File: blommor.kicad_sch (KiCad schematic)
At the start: 43 parts

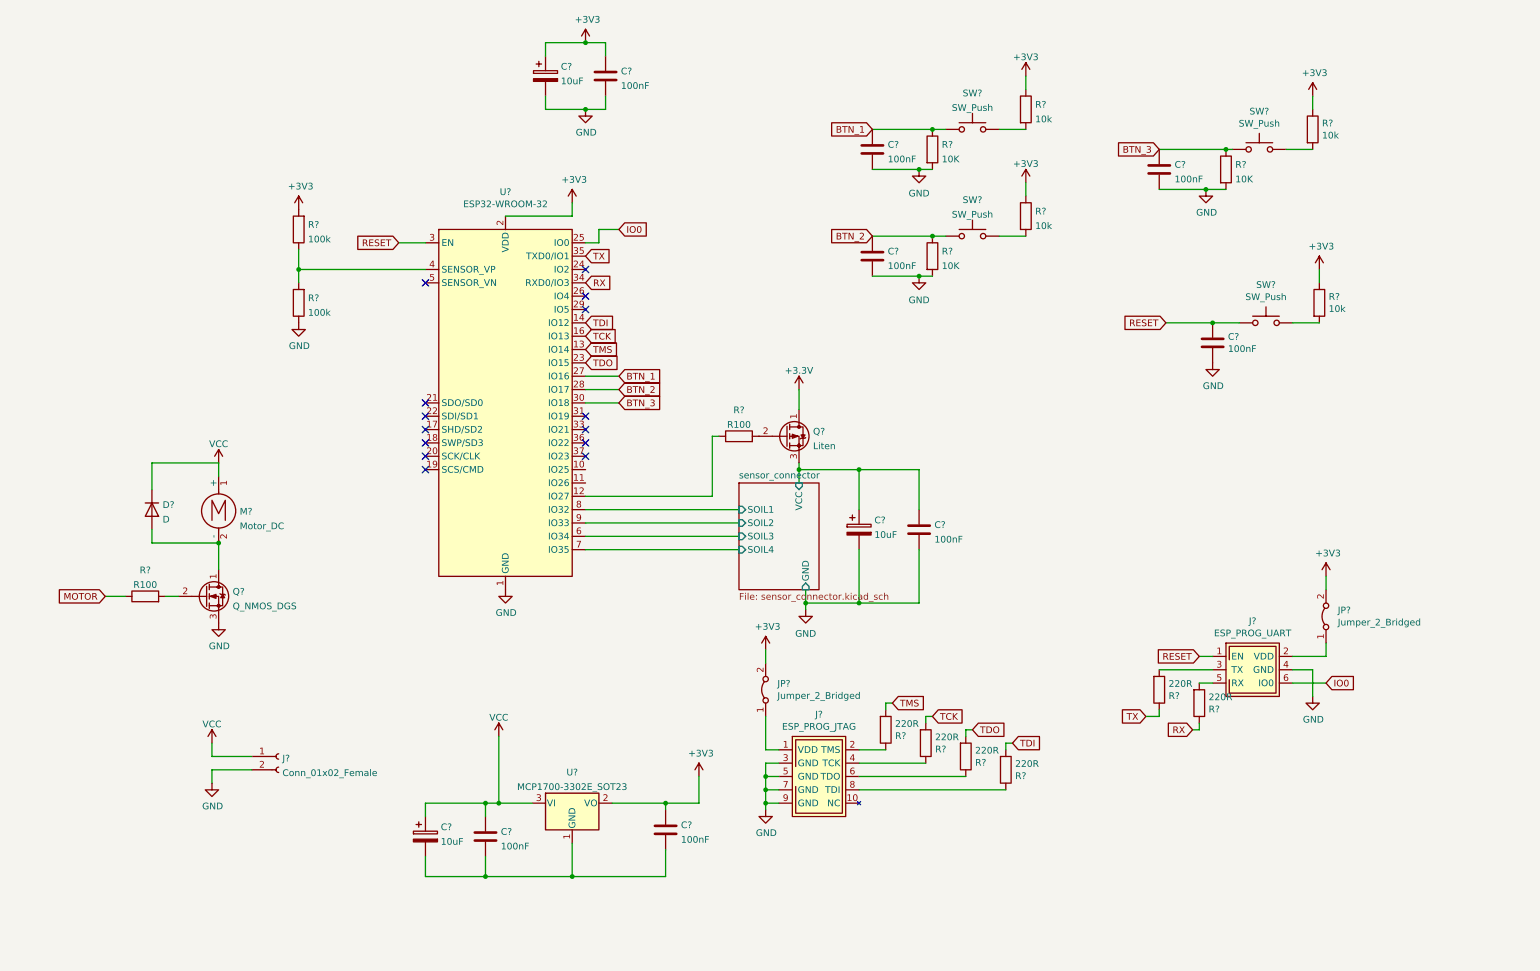
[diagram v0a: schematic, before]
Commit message: Added Amplifier board om "special" lib. Added Amplifier to board with shutdown pins. Added DHT11 sensor to sensor schematic. Updated connector lib.
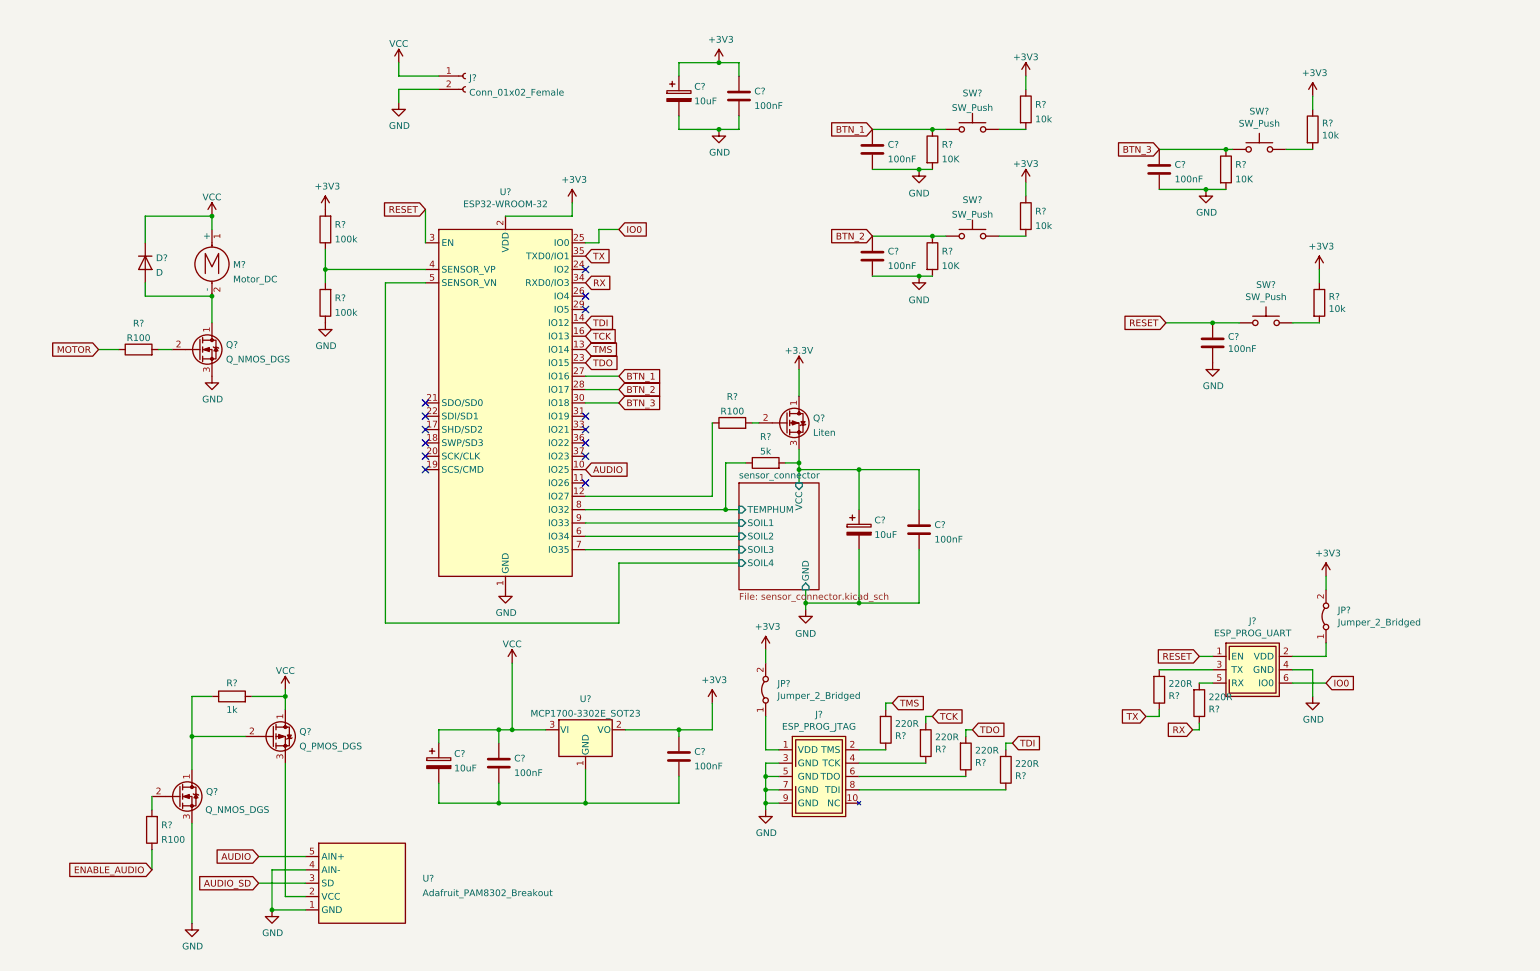
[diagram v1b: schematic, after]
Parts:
- removed SW?: SW_Push, Button_Switch_SMD:SW_SPST_TL3342, symbol Switch:SW_Push
- added Q?: Q_PMOS_DGS, symbol Device:Q_PMOS_DGS
- added Q?: Q_NMOS_DGS, symbol Device:Q_NMOS_DGS
- added R?: 1k, symbol Device:R
- added R?: 5k, symbol Device:R
- added R?: R100, symbol Device:R
- added SW?: SW_Push, Button_Switch_THT:SW_PUSH_6mm_H5mm, symbol Switch:SW_Push
- added U?: Adafruit_PAM8302_Breakout, special:Adafruit_PAM8302_Breakout, symbol special:Adafruit_PAM8302_Breakout
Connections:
- net GND: now also Q?.3 (S), U?.1 (GND), U?.4 (AIN-)
- net RESET: now also SW?.1
- net VCC: now also Q?.1 (D), R?.2
- net sensor_connector/SOIL1: now also U?.9 (IO33); no longer U?.8 (IO32)
- net sensor_connector/SOIL2: now also U?.6 (IO34); no longer U?.9 (IO33)
- net sensor_connector/SOIL3: now also U?.7 (IO35); no longer U?.6 (IO34)
- net sensor_connector/SOIL4: now also U?.5 (SENSOR_VN); no longer U?.7 (IO35)
- net sensor_connector/VCC: now also R?.2
- net at R?.2: now also SW?.2
- net AUDIO: now reaches U?.10 (IO25)
- net AUDIO: now also U?.5 (AIN+)
- new net: Q?.1 (D), Q?.2 (G), R?.1
- new net: Q?.2 (G), R?.2
- new net: Q?.3 (S), U?.2 (VCC)
- new net AUDIO_SD: U?.3 (SD)
- new net ENABLE_AUDIO: R?.1
- new net sensor_connector/TEMPHUM: R?.1, U?.8 (IO32)
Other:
- sheet sensor_connector ports: added TEMPHUM; removed none
- moved on the sheet: C?, D?, J?, M?, Q?, R?, U?

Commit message: Corrected RESET curcit to not keep the device in reset state. Added more capacitors to be a buffer for the motor. Added fuse to motor.
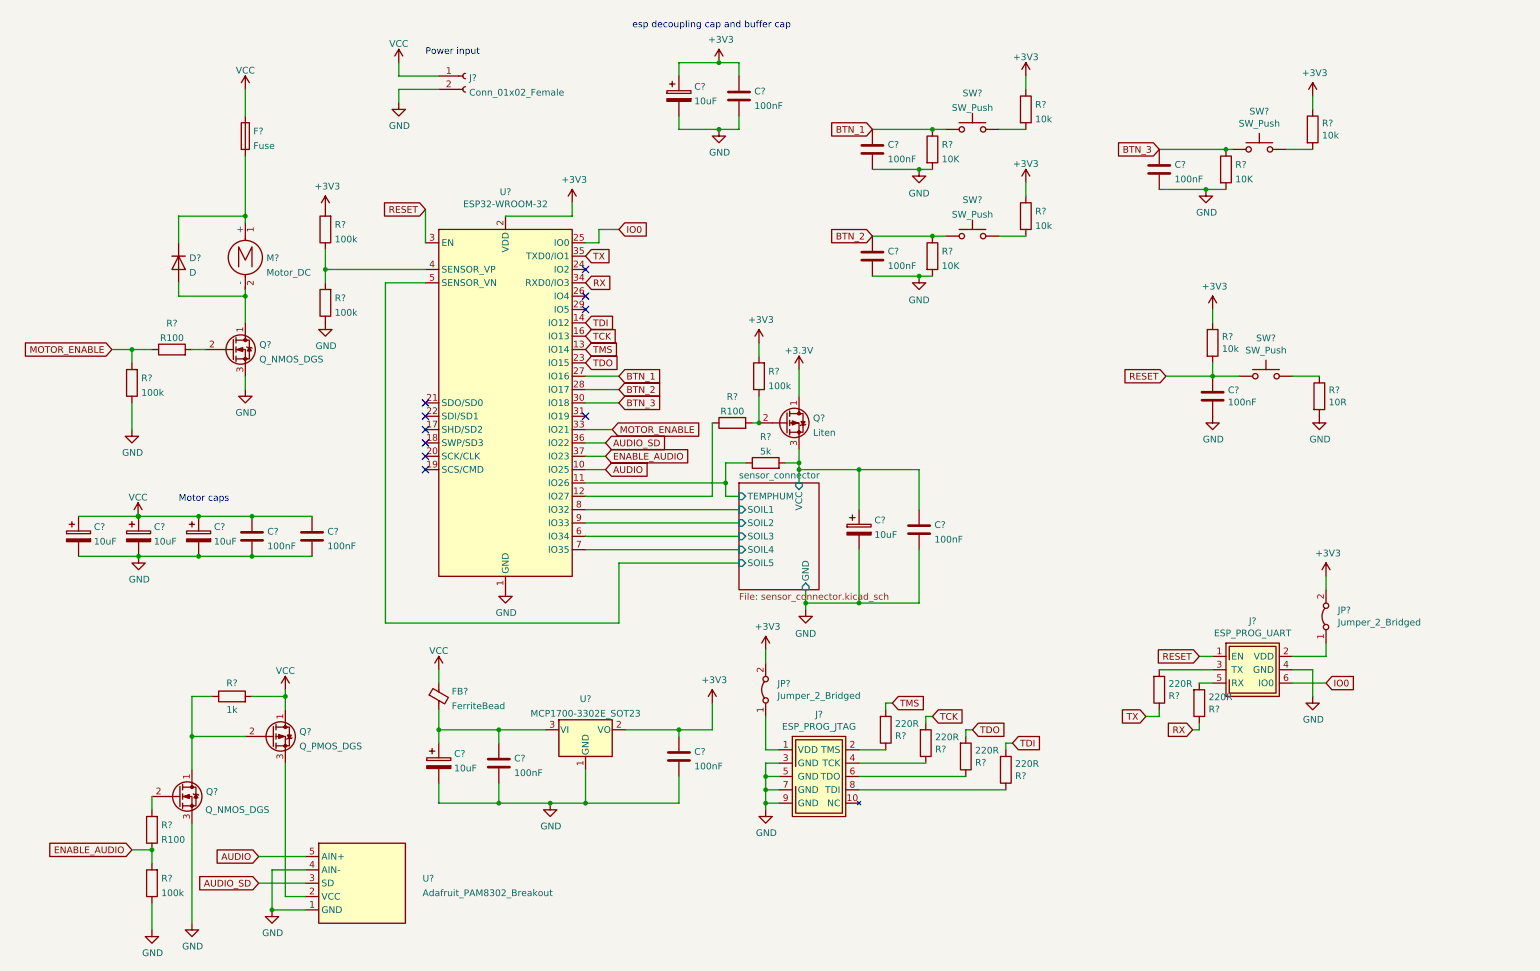
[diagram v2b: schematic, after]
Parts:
- added C? (x2): 100nF, symbol Device:C
- added C? (x3): 10uF, symbol Device:C_Polarized
- added F?: Fuse, Fuse:Fuseholder_Cylinder-5x20mm_Stelvio-Kontek_PTF78_Horizontal_Open, symbol Device:Fuse
- added FB?: FerriteBead, Resistor_SMD:R_1206_3216Metric_Pad1.30x1.75mm_HandSolder, symbol Device:FerriteBead_Small
- added R?: 10k, Resistor_SMD:R_0603_1608Metric_Pad0.98x0.95mm_HandSolder, symbol Device:R
- added R? (x3): 100k, symbol Device:R
- R?: value 10k -> 10R
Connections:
- net MOTOR is gone; now on net MOTOR_ENABLE: R?.1
- net +3V3: now also R?.1, R?.2; no longer R?.1
- net AUDIO_SD: now also U?.36 (IO22)
- net ENABLE_AUDIO: now also U?.37 (IO23), R?.2
- net GND: now also C?.2, C?.2, C?.2, R?.2, U?.1 (GND), C?.2, C?.2, C?.2, C?.2, C?.2, R?.1, R?.1
- net RESET: now also R?.2
- net VCC: now also C?.1, C?.1, C?.1, C?.1, C?.1, F?.1, FB?.1; no longer C?.1, C?.1, D?.1 (K), M?.1 (+), U?.3 (VI)
- net sensor_connector/SOIL1: now also U?.8 (IO32); no longer U?.9 (IO33)
- net sensor_connector/SOIL2: now also U?.9 (IO33); no longer U?.6 (IO34)
- net sensor_connector/SOIL3: now also U?.6 (IO34); no longer U?.7 (IO35)
- net sensor_connector/SOIL4: now also U?.7 (IO35); no longer U?.5 (SENSOR_VN)
- net sensor_connector/TEMPHUM: now also U?.11 (IO26); no longer U?.8 (IO32)
- net at Q?.2 (G), R?.2: now also R?.1
- net at SW?.2: now also R?.1; no longer R?.2
- net MOTOR_ENABLE: now reaches U?.33 (IO21)
- net MOTOR_ENABLE: now also R?.2
- new net: C?.1, C?.1, FB?.2, U?.3 (VI)
- new net: D?.1 (K), F?.2, M?.1 (+)
- new net sensor_connector/SOIL5: U?.5 (SENSOR_VN)
- no-connect marks 14 -> 10
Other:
- sheet sensor_connector ports: added SOIL5; removed none
- note added: "Motor caps"
- note added: "Power input"
- note added: "esp decoupling cap and buffer cap"
- moved on the sheet: C?, D?, M?, Q?, R?, SW?

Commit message: Added pcb, not routed but sorted. Gave all footprints refernces. Missing some footprints or might be wrong.
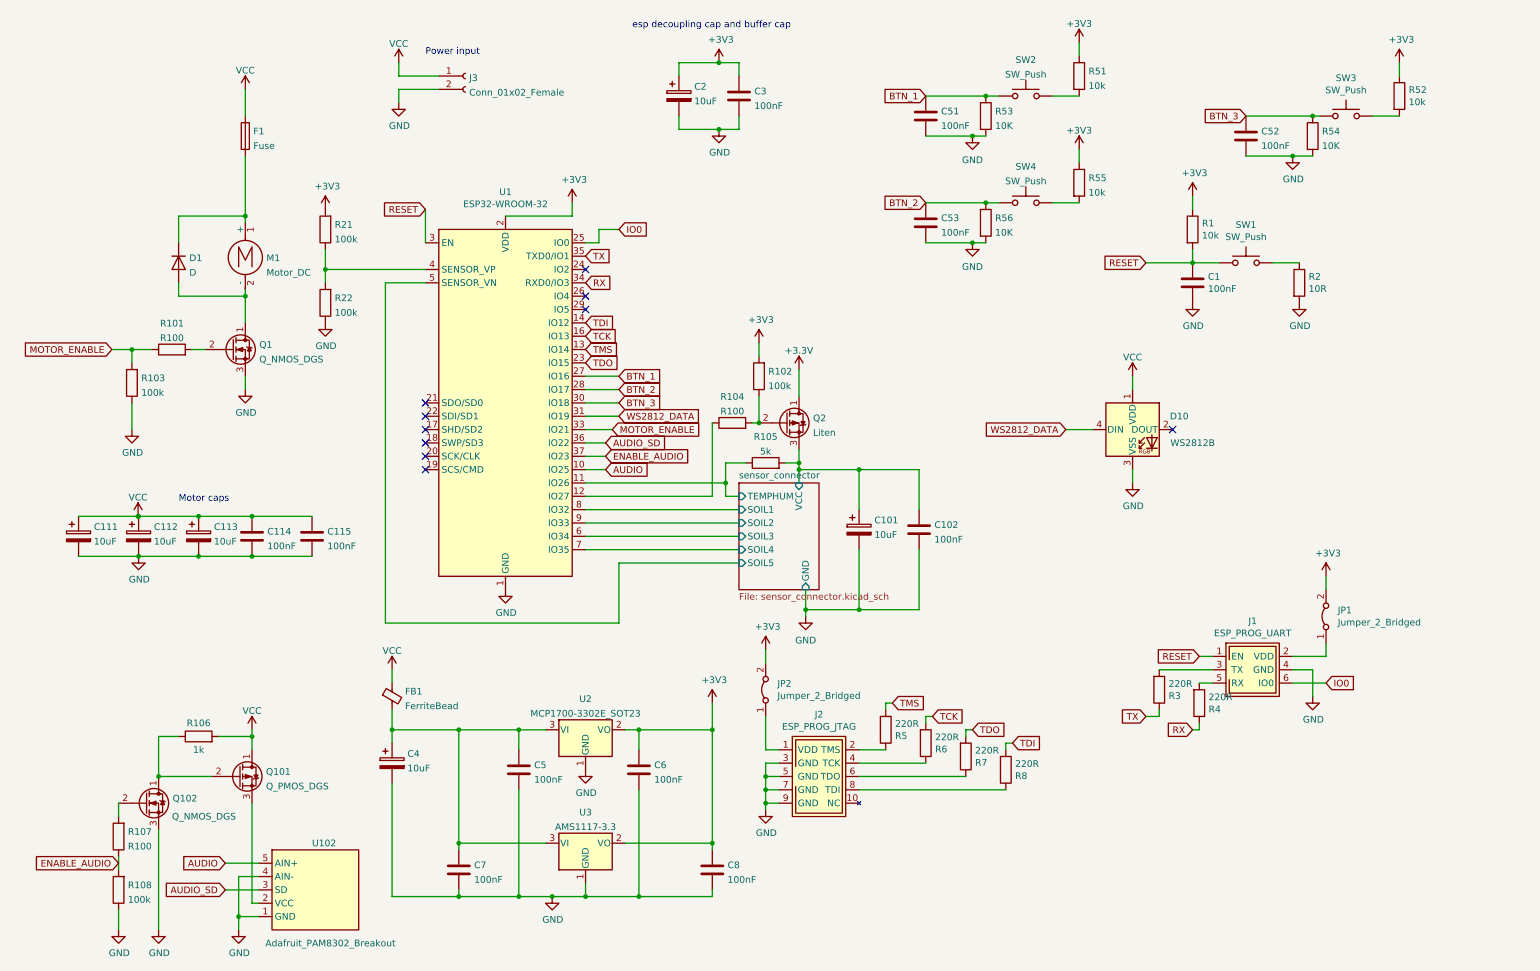
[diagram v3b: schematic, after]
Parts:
- added C7, C8: 100nF, Capacitor_SMD:C_0603_1608Metric_Pad1.08x0.95mm_HandSolder, symbol Device:C
- added D10: WS2812B, LED_SMD:LED_WS2812B_PLCC4_5.0x5.0mm_P3.2mm, symbol LED:WS2812B
- added U3: AMS1117-3.3, Package_TO_SOT_SMD:SOT-223-3_TabPin2, symbol Regulator_Linear:AMS1117-3.3
- C1, C51, C52, C53: renamed from C?; footprint Capacitor_SMD:C_0603_1608Metric -> Capacitor_SMD:C_0603_1608Metric_Pad1.08x0.95mm_HandSolder
- C101, C111, C112, C113, C2, C4: renamed from C?; footprint (none) -> Capacitor_SMD:CP_Elec_8x10.5
- C102, C114, C115, C3, C5, C6: renamed from C?; footprint (none) -> Capacitor_SMD:C_0603_1608Metric_Pad1.08x0.95mm_HandSolder
- D1: renamed from D?; footprint (none) -> Diode_THT:D_DO-15_P15.24mm_Horizontal
- M1: renamed from M?; footprint Connector_PinHeader_2.54mm:PinHeader_1x02_P2.54mm_Vertical -> Connector_JST:JST_XH_B2B-XH-A_1x02_P2.50mm_Vertical
- R101, R102, R103, R104, R105, R106, R107, R108, R21, R22: renamed from R?; footprint (none) -> Resistor_SMD:R_0603_1608Metric_Pad0.98x0.95mm_HandSolder
- gave numbers to parts that had none: 32
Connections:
- net +3V3: now also C8.1, U3.2 (VO)
- net GND: now also C7.2, C8.2, D10.3 (VSS), U3.1 (GND)
- net VCC: now also D10.1 (VDD)
- net at C4.1, C5.1, FB1.2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: now also C7.1, U3.3 (VI)
- net WS2812_DATA: now reaches U1.31 (IO19)
- net WS2812_DATA: now also D10.4 (DIN)
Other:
- title: (none) -> Flower watering thinga-ma-bob
- moved on the sheet: C1, C4, C5, C51, C52, C53, C6, FB1, Q101, Q102, R1, R106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

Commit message: Added OST logo.
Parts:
- added SILKSCREEN?: OSTSymbol, SymbolOST:ost-bubble_12mm_SilkScreen, symbol SymbolOST:OSTSymbol
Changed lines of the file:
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@@
     (pin "2")
+  )
+  (symbol (lib_id "SymbolOST:OSTSymbol") (at 274.32 173.99 0) (unit 1)
+    (in_bom no) (on_board yes)
+    (property "Reference" "SILKSCREEN?" (id 0) (at 283.21 172.72 0)
+      (effects (font (size 1.27 1.27)) (justify left))
+    )
+    (property "Value" "OSTSymbol" (id 1) (at 284.48 175.26 0)
+      (effects (font (size 1.27 1.27)) (justify left))
+    )
+    (property "Footprint" "SymbolOST:ost-bubble_12mm_SilkScreen" (id 2) (at 274.32 173.99 0)
+      (effects (font (size 1.27 1.27)) hide)
+    )
+    (property "Datasheet" "" (id 3) (at 274.32 173.99 0)
+      (effects (font (size 1.27 1.27)) hide)
+    )
   )
   (symbol (lib_id "power:GND") (at 33.02 118.11 0) (unit 1)
@@
       (reference "R108") (unit 1) (value "100k") (footprint "Resistor_SMD:R_0603_1608Metric_Pad0.98x0.95mm_HandSolder")
     )
+    (path "/20481654-b937-4da0-8104-556bc4355376"
+      (reference "SILKSCREEN?") (unit 1) (value "OSTSymbol") (footprint "SymbolOST:ost-bubble_12mm_SilkScreen")
+    )
     (path "/e2f633a2-7424-4a96-b983-ef3c5f1e2aef"

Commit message: Forgot to save...
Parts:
- gave numbers to parts that had none: 1
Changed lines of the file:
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@@
   (symbol (lib_id "SymbolOST:OSTSymbol") (at 274.32 173.99 0) (unit 1)
     (in_bom no) (on_board yes)
-    (property "Reference" "SILKSCREEN?" (id 0) (at 283.21 172.72 0)
+    (property "Reference" "SILKSCREEN1" (id 0) (at 283.21 172.72 0)
       (effects (font (size 1.27 1.27)) (justify left))
     )
@@
     )
     (path "/20481654-b937-4da0-8104-556bc4355376"
-      (reference "SILKSCREEN?") (unit 1) (value "OSTSymbol") (footprint "SymbolOST:ost-bubble_12mm_SilkScreen")
+      (reference "SILKSCREEN1") (unit 1) (value "OSTSymbol") (footprint "SymbolOST:ost-bubble_12mm_SilkScreen")
     )
     (path "/e2f633a2-7424-4a96-b983-ef3c5f1e2aef"

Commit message: Renamed ConnectorEsp folder so 3D models work. Started routing and more layout work.
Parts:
- added C11: 100nF, Capacitor_SMD:C_0603_1608Metric_Pad1.08x0.95mm_HandSolder, symbol Device:C
- SW1: footprint Button_Switch_THT:SW_PUSH_6mm_H5mm -> Button_Switch_SMD:SW_SPST_TL3342
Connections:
- net AUDIO_SD: now also U1.31 (IO19); no longer U1.36 (IO22)
- net BTN_1: now also U1.28 (IO17); no longer U1.27 (IO16)
- net BTN_2: now also U1.29 (IO5); no longer U1.28 (IO17)
- net ENABLE_AUDIO: now also U1.33 (IO21); no longer U1.37 (IO23)
- net GND: now also C11.2
- net MOTOR_ENABLE: now also U1.26 (IO4); no longer U1.33 (IO21)
- net VCC: now also C11.1
- net WS2812_DATA: now also U1.37 (IO23); no longer U1.31 (IO19)
- net sensor_connector/SOIL1: now also U1.9 (IO33); no longer U1.8 (IO32)
- net sensor_connector/SOIL2: now also U1.8 (IO32); no longer U1.9 (IO33)
- net sensor_connector/SOIL3: now also U1.7 (IO35); no longer U1.6 (IO34)
- net sensor_connector/SOIL4: now also U1.6 (IO34); no longer U1.7 (IO35)
- net SENSOR_POWER_EN: now reaches R104.1, U1.12 (IO27)
- net sensor_connector/VCC renamed sensor_connector/SENS_VCC
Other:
- sheet sensor_connector ports: added SENS_VCC; removed VCC

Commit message: Typ klar nu.
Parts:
- C101, C111, C112, C113, C2, C4: footprint Capacitor_SMD:CP_Elec_8x10.5 -> Capacitor_SMD:CP_Elec_10x10.5
- Q1: value Q_NMOS_DGS -> IPS021L; footprint (none) -> Package_TO_SOT_SMD:SOT-223-3_TabPin2; symbol Device:Q_NMOS_DGS -> Device:Q_NMOS_GDS
- Q101: value Q_PMOS_DGS -> A1SHB; footprint (none) -> Package_TO_SOT_SMD:SOT-23; symbol Device:Q_PMOS_DGS -> Device:Q_PMOS_GSD
- Q102: value Q_NMOS_DGS -> BST82-1; footprint (none) -> Package_TO_SOT_SMD:SOT-23; symbol Device:Q_NMOS_DGS -> Device:Q_NMOS_GSD
- Q2: value Liten -> A1SHB; footprint (none) -> Package_TO_SOT_SMD:SOT-23
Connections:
- net BTN_1: now also U1.26 (IO4); no longer U1.28 (IO17)
- net BTN_2: now also U1.30 (IO18); no longer U1.29 (IO5)
- net BTN_3: now also U1.27 (IO16); no longer U1.30 (IO18)
- net GND: now also Q102.2 (S); no longer Q102.3 (S)
- net MOTOR_ENABLE: now also U1.28 (IO17); no longer U1.26 (IO4)
- net SENSOR_POWER_EN: now also U1.11 (IO26); no longer U1.12 (IO27)
- net VCC: now also Q101.3 (D); no longer Q101.1 (D)
- net sensor_connector/TEMPHUM: now also U1.12 (IO27); no longer U1.11 (IO26)
- net at R107.2: now also Q102.1 (G); no longer Q102.2 (G)
- net at U102.2 (VCC): now also Q101.2 (S); no longer Q101.3 (S)
- net at R101.2: now also Q1.1 (G); no longer Q1.2 (G)
- net at D1.2 (A), M1.2 (-): now also Q1.2 (D); no longer Q1.1 (D)
- new net: Q101.1 (G), Q102.3 (D), R106.1

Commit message: Saker saker saker.... PALLA
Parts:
- added J51, J52, J53: Conn_01x01_Female, Connector_PinSocket_2.54mm:PinSocket_1x01_P2.54mm_Vertical, symbol Connector:Conn_01x01_Female
- added J54: Conn_01x03_Female, Connector_PinSocket_2.54mm:PinSocket_1x03_P2.54mm_Vertical, symbol Connector:Conn_01x03_Female
- added J55, J56: Conn_01x02_Female, Connector_PinSocket_2.54mm:PinSocket_1x02_P2.54mm_Vertical, symbol Connector:Conn_01x02_Female
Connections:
- net +3V3: now also J55.1 (Pin_1), J55.2 (Pin_2)
- net GND: now also J54.1 (Pin_1), J54.2 (Pin_2), J54.3 (Pin_3)
- net VCC: now also J56.1 (Pin_1), J56.2 (Pin_2)
- net at U1.24 (IO2): now also J51.1 (Pin_1)
- net at U1.29 (IO5): now also J52.1 (Pin_1)
- net at U1.36 (IO22): now also J53.1 (Pin_1)
- no-connect marks 10 -> 7
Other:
- moved on the sheet: C2, C3, J3, Q2, R102, R104
